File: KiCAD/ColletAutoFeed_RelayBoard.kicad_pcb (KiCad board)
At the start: 2 copper layers, 139.7 x 111.8 mm, 55 parts, among them J1 1761685-6, J2 2068320202, K1 G5V-1, K2 G5V-1, K3 G5V-1, K4 G5V-1, K5 G5V-1, K6 G5V-1, K7 G5V-1, K8 G5V-1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

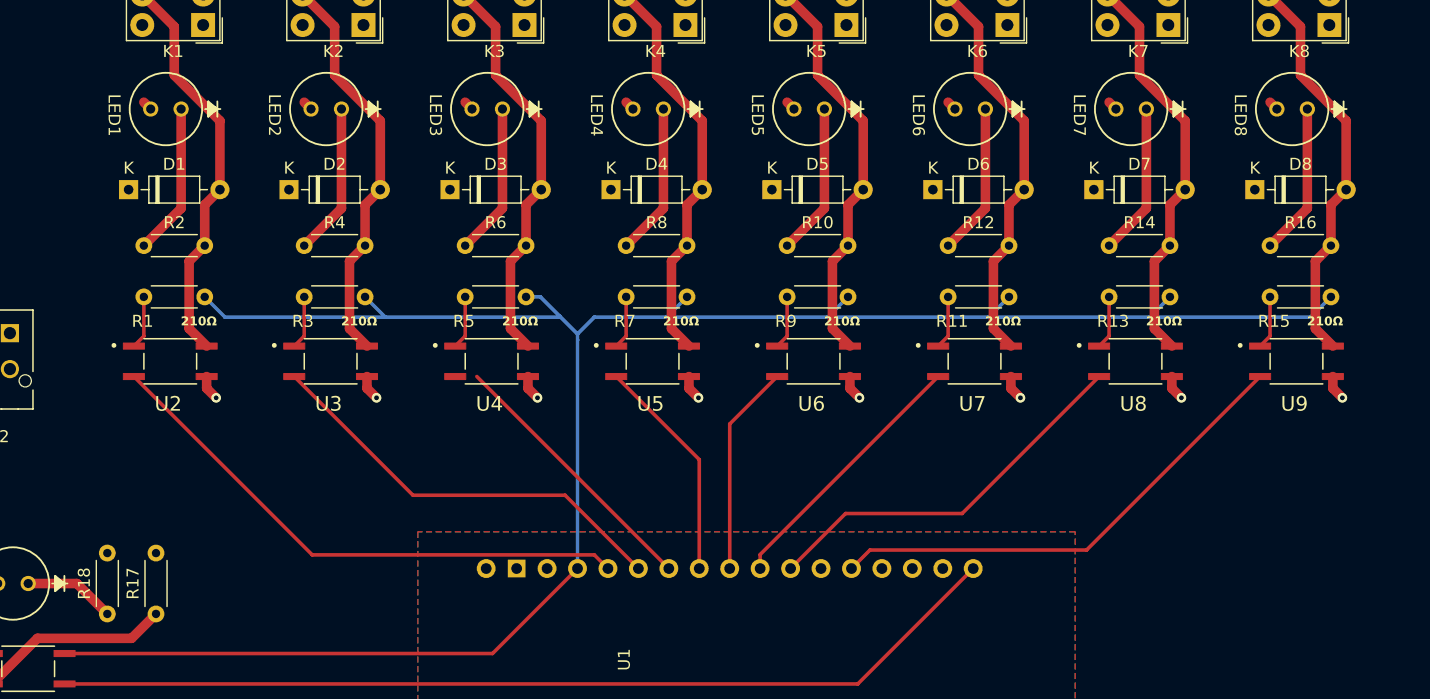
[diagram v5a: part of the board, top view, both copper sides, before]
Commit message: Updated resistor footprints to include values
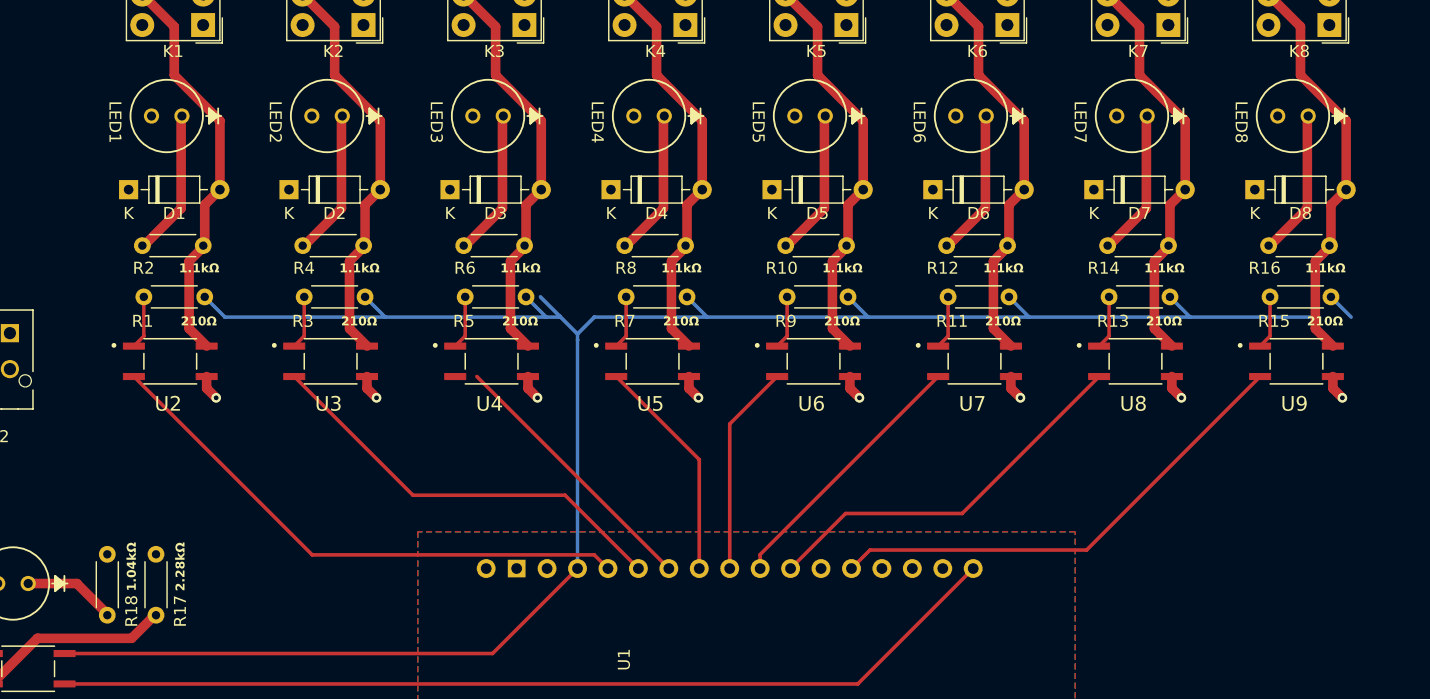
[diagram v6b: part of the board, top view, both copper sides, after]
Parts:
- R10, R12, R14, R16, R17, R18, R2, R4, R6, R8: footprint Resistor_THT:R_Axial_DIN0204_L3.6mm_D1.6mm_P5.08mm_Horizontal -> Resistor:R_Axial_DIN0204_L3.6mm_D1.6mm_P5.08mm_Horizontal-JW
- moved R17 4.98 mm to (99.7, 111.8), turned to -90 degrees
- moved R18 4.98 mm to (95.6, 111.8), turned to -90 degrees
- moved LED1 0.59 mm to (101.9, 75.2)
- moved LED2 0.59 mm to (115.2, 75.2)
- moved LED3 0.59 mm to (128.7, 75.2)
- moved LED4 0.59 mm to (142.1, 75.2)
- moved LED5 0.59 mm to (155.5, 75.2)
- moved LED6 0.59 mm to (169.0, 75.2)
- moved LED7 0.59 mm to (182.4, 75.2)
- moved LED8 0.59 mm to (195.8, 75.2)
- moved R10 0.12 mm to (152.2, 86.0)
- moved R12 0.12 mm to (165.7, 86.0)
- moved R2 0.12 mm to (98.6, 86.0)
- moved R4 0.12 mm to (111.9, 86.0)
- moved R6 0.12 mm to (125.4, 86.0)
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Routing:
- net +24V: track 7.96 -> 1.50 mm
- net /MCU 3.3v: track 177.3 -> 178.5 mm
- net Net-(LED8-Pad1): track 12.7 -> 12.1 mm
- net Net-(LED7-Pad1): track 12.7 -> 12.1 mm
- net Net-(LED6-Pad1): track 12.7 -> 12.1 mm
- net Net-(LED5-Pad1): track 12.7 -> 12.1 mm
- net Net-(LED4-Pad1): track 12.7 -> 12.1 mm
- net Net-(LED3-Pad1): track 12.7 -> 12.1 mm
- net Net-(LED2-Pad1): track 12.7 -> 12.1 mm
- net Net-(LED1-Pad1): track 12.7 -> 12.1 mm

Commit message: Replaced ribbon cable connector with 10-pin molex
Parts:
- removed J2: 2068320202, Molex 206832-0202:MOLEX_2068320202
- J1: value 1761685-6 -> XW4M-10D2-H1DS; footprint Vertical Header - Locking:TE_1761685-6 -> xw4m-10d2-h1ds:xw4m-10d2-h1ds
- moved J1 54.3 mm to (89.7, 68.1), turned to -90 degrees
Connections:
- J1 pad 11: /S6 -> (no net)
- J1 pad 12: GND -> (no net)
- J1 pad 2: GND -> /S2
- J1 pad 3: /S2 -> /S3
- J1 pad 4: GND -> /S4
- J1 pad 5: /S3 -> /S5
- J1 pad 6: GND -> /S6
- J1 pad 7: /S4 -> /S7
- J1 pad 8: GND -> /S8
- J1 pad 9: /S5 -> +24V

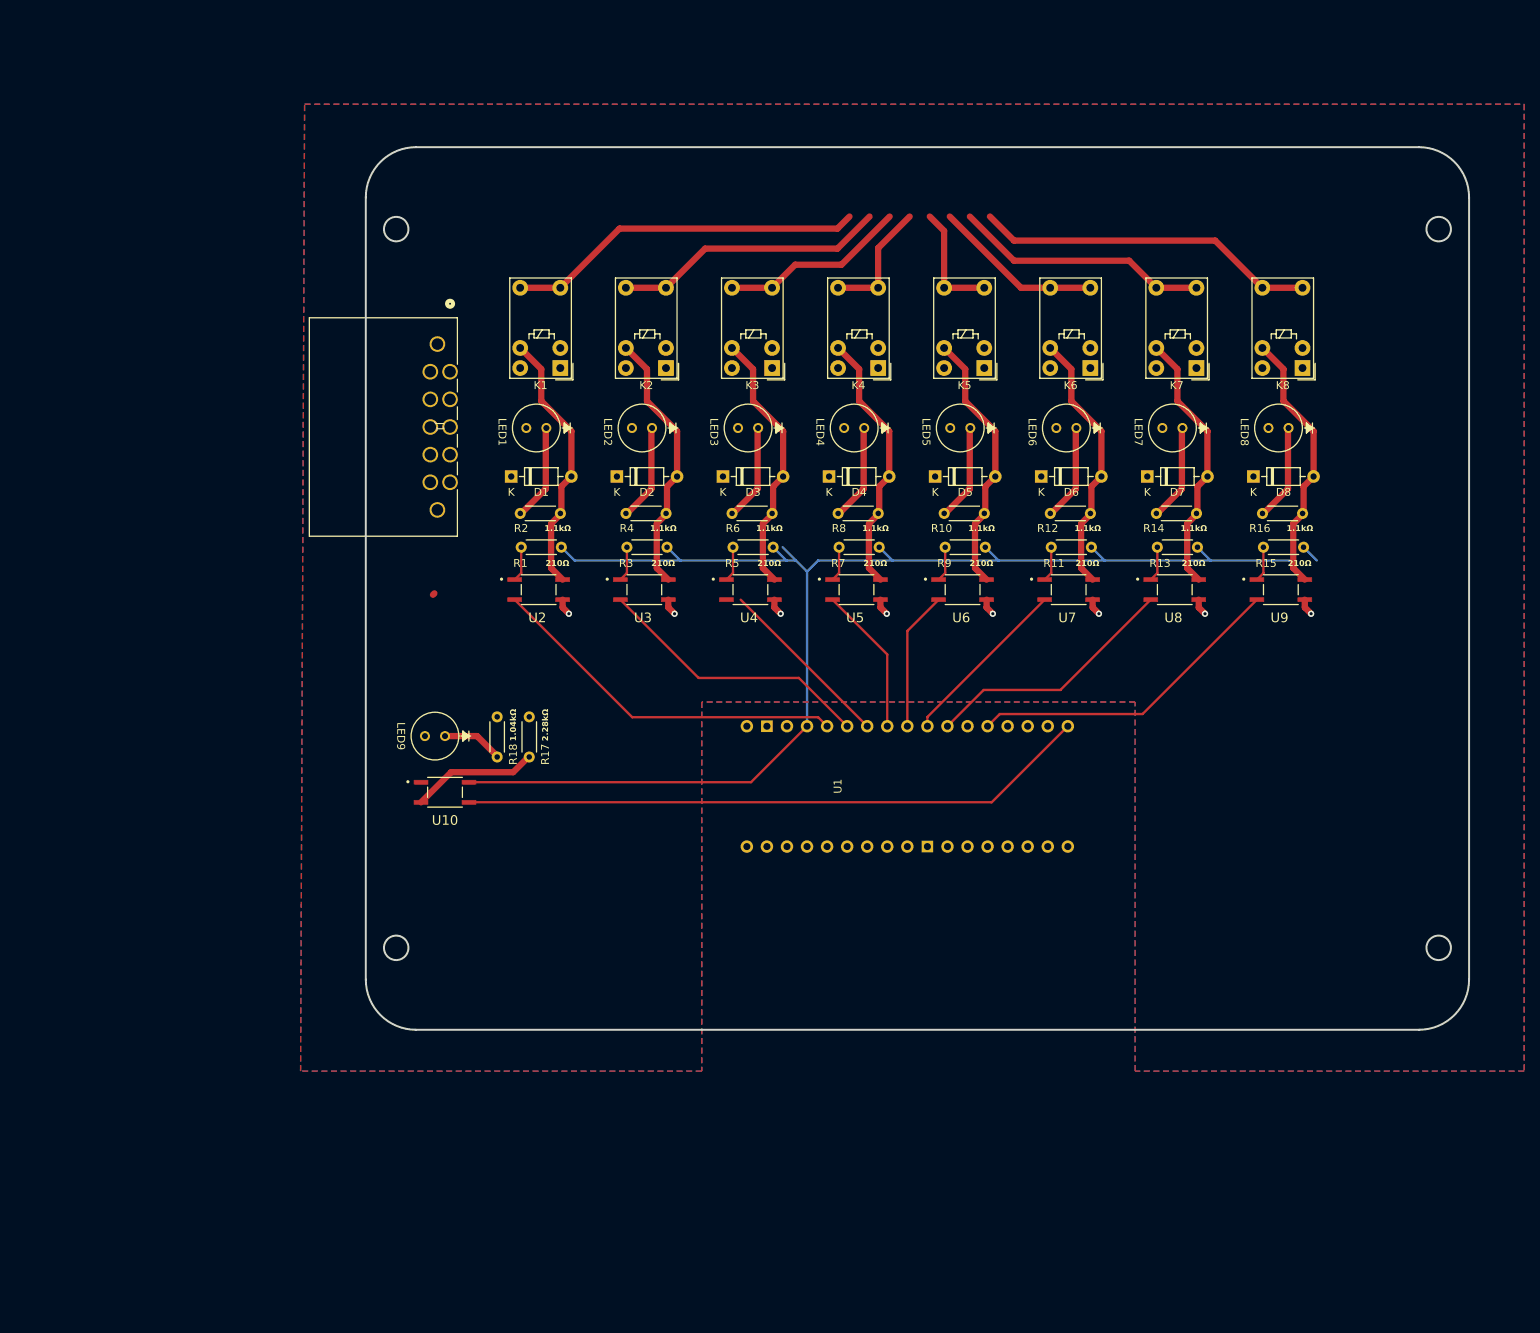
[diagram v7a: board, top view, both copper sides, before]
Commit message: Updated board to new size
Updated board outline, stripped all old routing, added 2 pin omron power connector
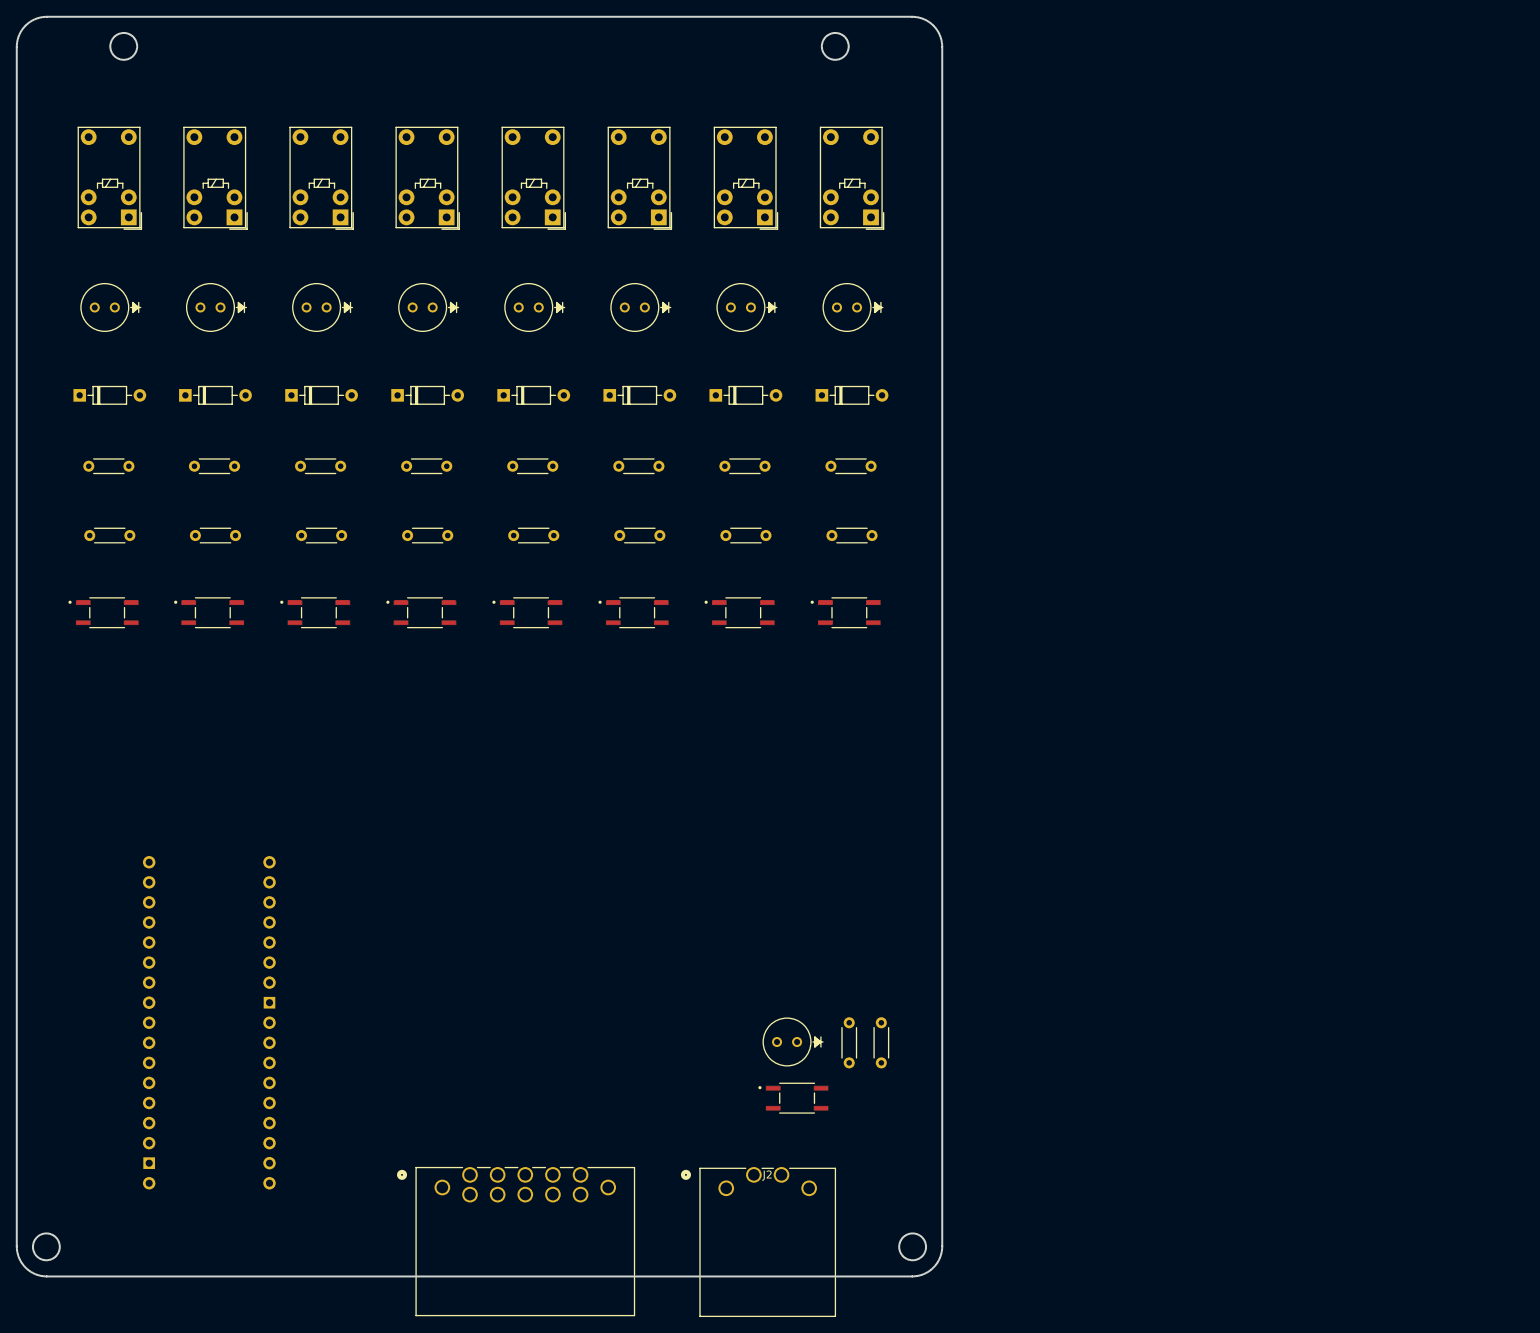
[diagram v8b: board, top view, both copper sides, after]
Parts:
- added J2: XW4M-02D1-H1DA, xw4m-02d1-h1da:xw4m-02d1-h1da, F.Cu at (128.1, 169.8)
- moved J1 101.7 mm to (92.2, 169.8), turned to 0 degrees
- moved U1 93.3 mm to (59.2, 150.5), turned to 180 degrees
- moved LED9 59.1 mm to (133.6, 152.9)
- moved U10 59.1 mm to (133.6, 160.0)
- moved R17 59.1 mm to (144.3, 150.5)
- moved R18 59.1 mm to (140.2, 150.5)
- moved K4 57.9 mm to (89.2, 48.5)
- moved K7 57.9 mm to (129.5, 48.5)
- moved K2 57.9 mm to (62.4, 48.5)
- moved K1 57.9 mm to (49.0, 48.5)
- moved K3 57.9 mm to (75.8, 48.5)
- moved K5 57.9 mm to (102.7, 48.5)
- moved K6 57.9 mm to (116.1, 48.5)
- moved K8 57.9 mm to (143.0, 48.5)
- moved LED3 56.7 mm to (74.0, 59.9)
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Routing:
- net /MCU 3.3v: track 178.5 -> 0.00 mm
- net /IO12: track 79.8 -> 0.00 mm
- net /IO1: track 46.2 -> 0.00 mm
- net /S1: track 45.4 -> 0.00 mm
- net /S8: track 43.3 -> 0.00 mm
- net /IO16: track 40.7 -> 0.00 mm
- net /IO2: track 35.4 -> 0.00 mm
- net /S2: track 34.6 -> 0.00 mm
- net Net-(D7-A): track 33.7 -> 0.00 mm
- net Net-(D1-A): track 33.7 -> 0.00 mm
- net Net-(D3-A): track 33.7 -> 0.00 mm
- net Net-(D8-A): track 33.7 -> 0.00 mm
- net Net-(D6-A): track 33.7 -> 0.00 mm
- net Net-(D5-A): track 33.7 -> 0.00 mm
- net Net-(D4-A): track 33.7 -> 0.00 mm
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- removed copper zone on F.Cu, net +24V
- removed copper zone on B.Cu, net GND
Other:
- board size 139.7 x 111.8 mm -> 117.2 x 159.5 mm
